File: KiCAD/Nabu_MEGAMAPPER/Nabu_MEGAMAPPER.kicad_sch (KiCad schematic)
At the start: 14 parts, among them J1 Z80 Socket Header, J2 Z80 Socket Header, U1 Z80CPU, U10 74LS374, U11 GAL22V10, U12 GAL22V10, U2 AS6C4008-55PCN, U3 74LS670, U4 74LS670, U5 HM6116, U6 74LS157, U7 74LS157, U8 74LS157, U9 74LS244

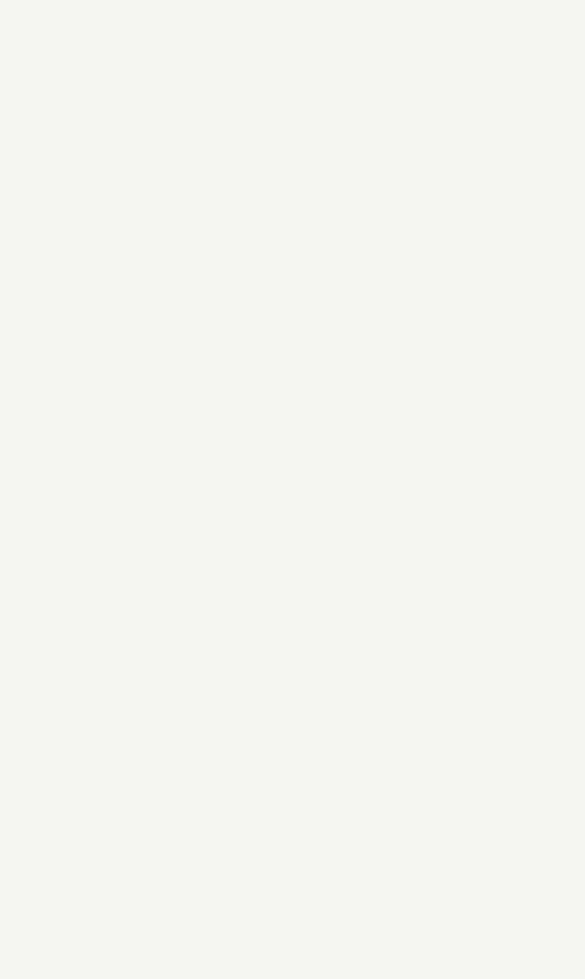
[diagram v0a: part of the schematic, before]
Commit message: Removed some of the 22V10s in favor of a CPLD
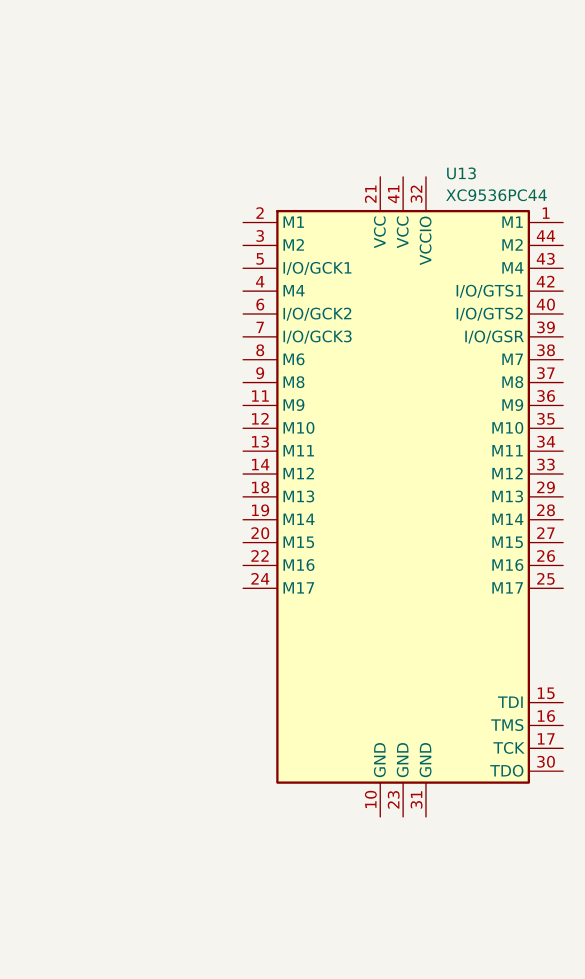
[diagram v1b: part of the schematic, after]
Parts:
- added U13: XC9536PC44, symbol CPLD_Xilinx:XC9536PC44
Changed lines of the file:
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@@
+    )
+  )
+  (symbol (lib_id "CPLD_Xilinx:XC9536PC44") (at 288.29 132.715 0) (unit 1)
+    (in_bom yes) (on_board yes) (dnp no) (fields_autoplaced)
+    (property "Reference" "U13" (at 293.0241 96.8207 0)
+      (effects (font (size 1.27 1.27)) (justify left))
+    )
+    (property "Value" "XC9536PC44" (at 293.0241 99.2449 0)
+      (effects (font (size 1.27 1.27)) (justify left))
+    )
+    (property "Footprint" "" (at 288.29 132.715 0)
+      (effects (font (size 1.27 1.27)) hide)
+    )
+    (property "Datasheet" "xilinx/xc9536.pdf" (at 288.29 132.715 0)
+      (effects (font (size 1.27 1.27)) hide)
+    )
+    (pin "1")
+    (pin "10")
+    (pin "11")
+    (pin "12")
+    (pin "13")
+    (pin "14")
+    (pin "15")
+    (pin "16")
+    (pin "17")
+    (pin "18")
+    (pin "19")
+    (pin "2")
+    (pin "20")
+    (pin "21")
+    (pin "22")
+    (pin "23")
+    (pin "24")
+    (pin "25")
+    (pin "26")
+    (pin "27")
+    (pin "28")
+    (pin "29")
+    (pin "3")
+    (pin "30")
+    (pin "31")
+    (pin "32")
+    (pin "33")
+    (pin "34")
+    (pin "35")
+    (pin "36")
+    (pin "37")
+    (pin "38")
+    (pin "39")
+    (pin "4")
+    (pin "40")
+    (pin "41")
+    (pin "42")
+    (pin "43")
+    (pin "44")
+    (pin "5")
+    (pin "6")
+    (pin "7")
+    (pin "8")
+    (pin "9")
+    (instances
+      (project "Nabu_MEGAMAPPER"
+        (path "/08a88c4b-5d36-43ed-bafe-b5ff1ee4c2dd"
+          (reference "U13") (unit 1)
+        )
+      )
     )
   )

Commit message: Continued work on schematic
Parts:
- removed U11, U12: GAL22V10, symbol Custom:GAL22V10
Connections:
- net *IORQ: now also U13.3 (M2)
- net *M1: now also U13.5 (I/O/GCK1)
- net *MREQ: now also U13.2 (M1)
- net *RESET: now also U13.39 (I/O/GSR)
- net +5V: now also U13.21 (VCC), U13.32 (VCCIO), U13.41 (VCC)
- net A10: now also U10.7 (D2)
- net A11: now also U10.8 (D3)
- net A12: now also U10.13 (D4)
- net A13: now also U10.14 (D5)
- net A14: now also U10.17 (D6)
- net A15: now also U10.18 (D7)
- net A8: now also U10.3 (D0)
- net A9: now also U10.4 (D1)
- net D0: now also U13.12 (M10); no longer U10.3 (D0)
- net D1: now also U13.13 (M11); no longer U10.4 (D1)
- net D2: now also U13.14 (M12); no longer U10.7 (D2)
- net D3: now also U13.18 (M13); no longer U10.8 (D3)
- net D4: now also U13.19 (M14); no longer U10.13 (D4)
- net D5: now also U13.20 (M15); no longer U10.14 (D5)
- net D6: now also U13.22 (M16); no longer U10.17 (D6)
- net D7: now also U13.24 (M17); no longer U10.18 (D7)
- net GND: now also U13.10 (GND), U13.23 (GND), U13.31 (GND)
- net *BNK_WR: now reaches U4.12 (~{Ew})
- net *BNK_WR: now also U3.12 (~{Ew})
- net *UA_OE: now reaches U10.1 (OE)
- net UA_CLK: now reaches U10.11 (Cp)
- net TRAP renamed A_TRAP
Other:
- moved on the sheet: U13

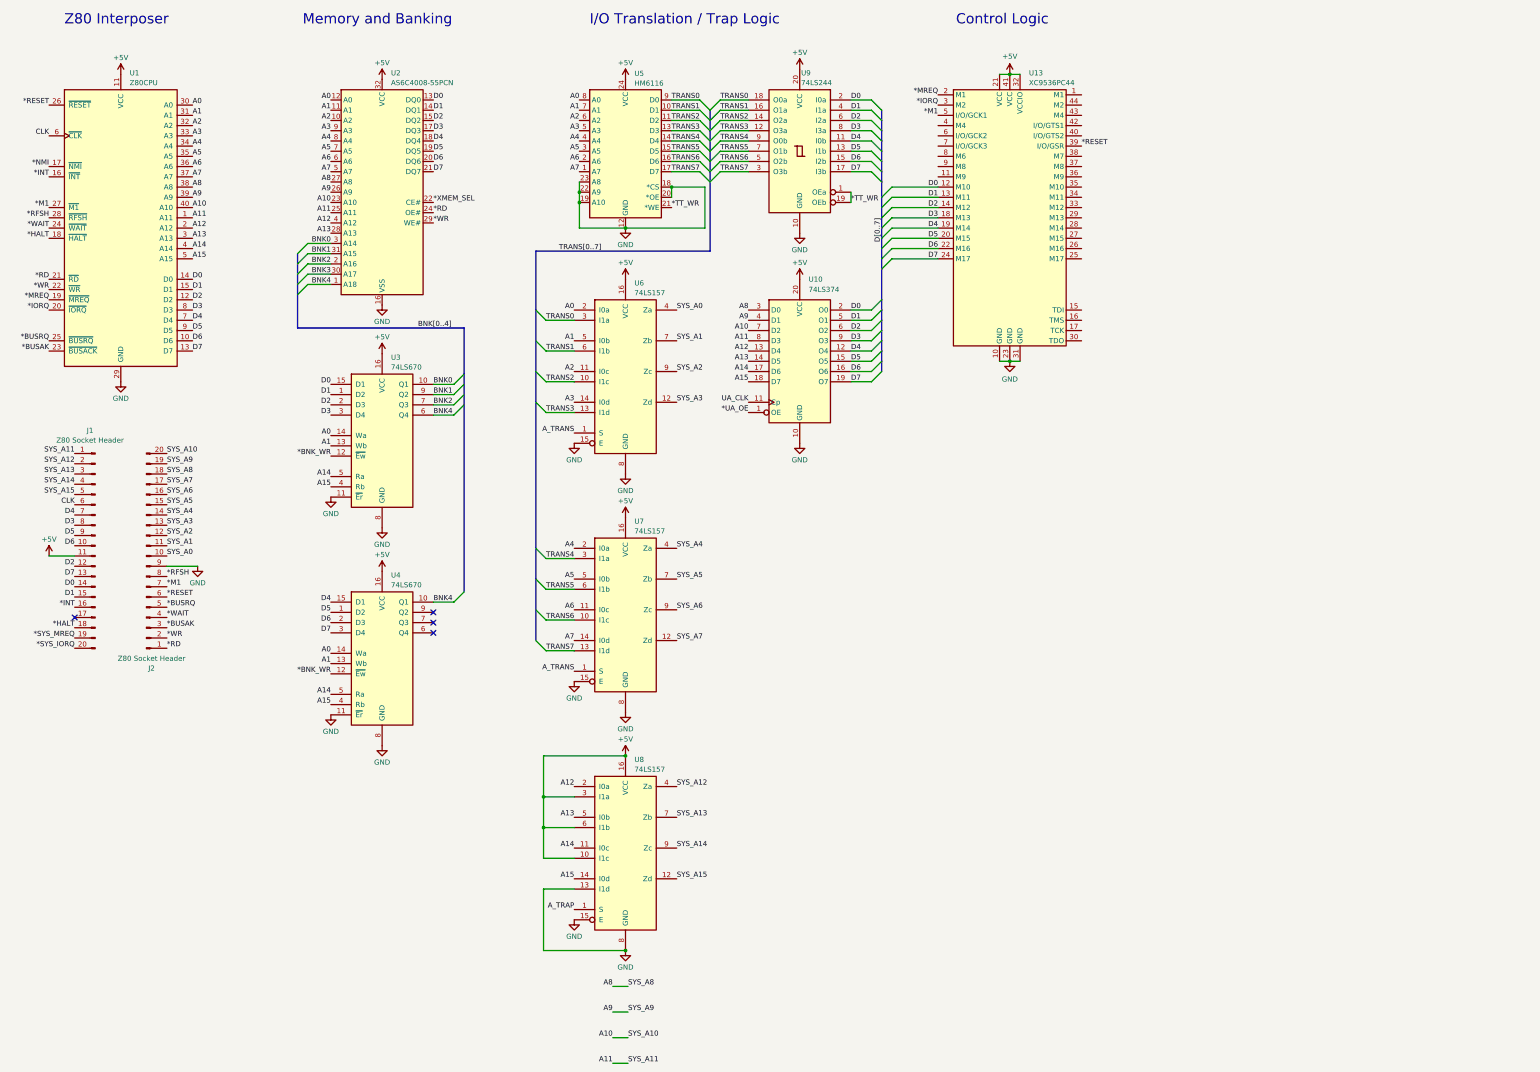
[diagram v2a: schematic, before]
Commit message: Added full address capture logic to schematic
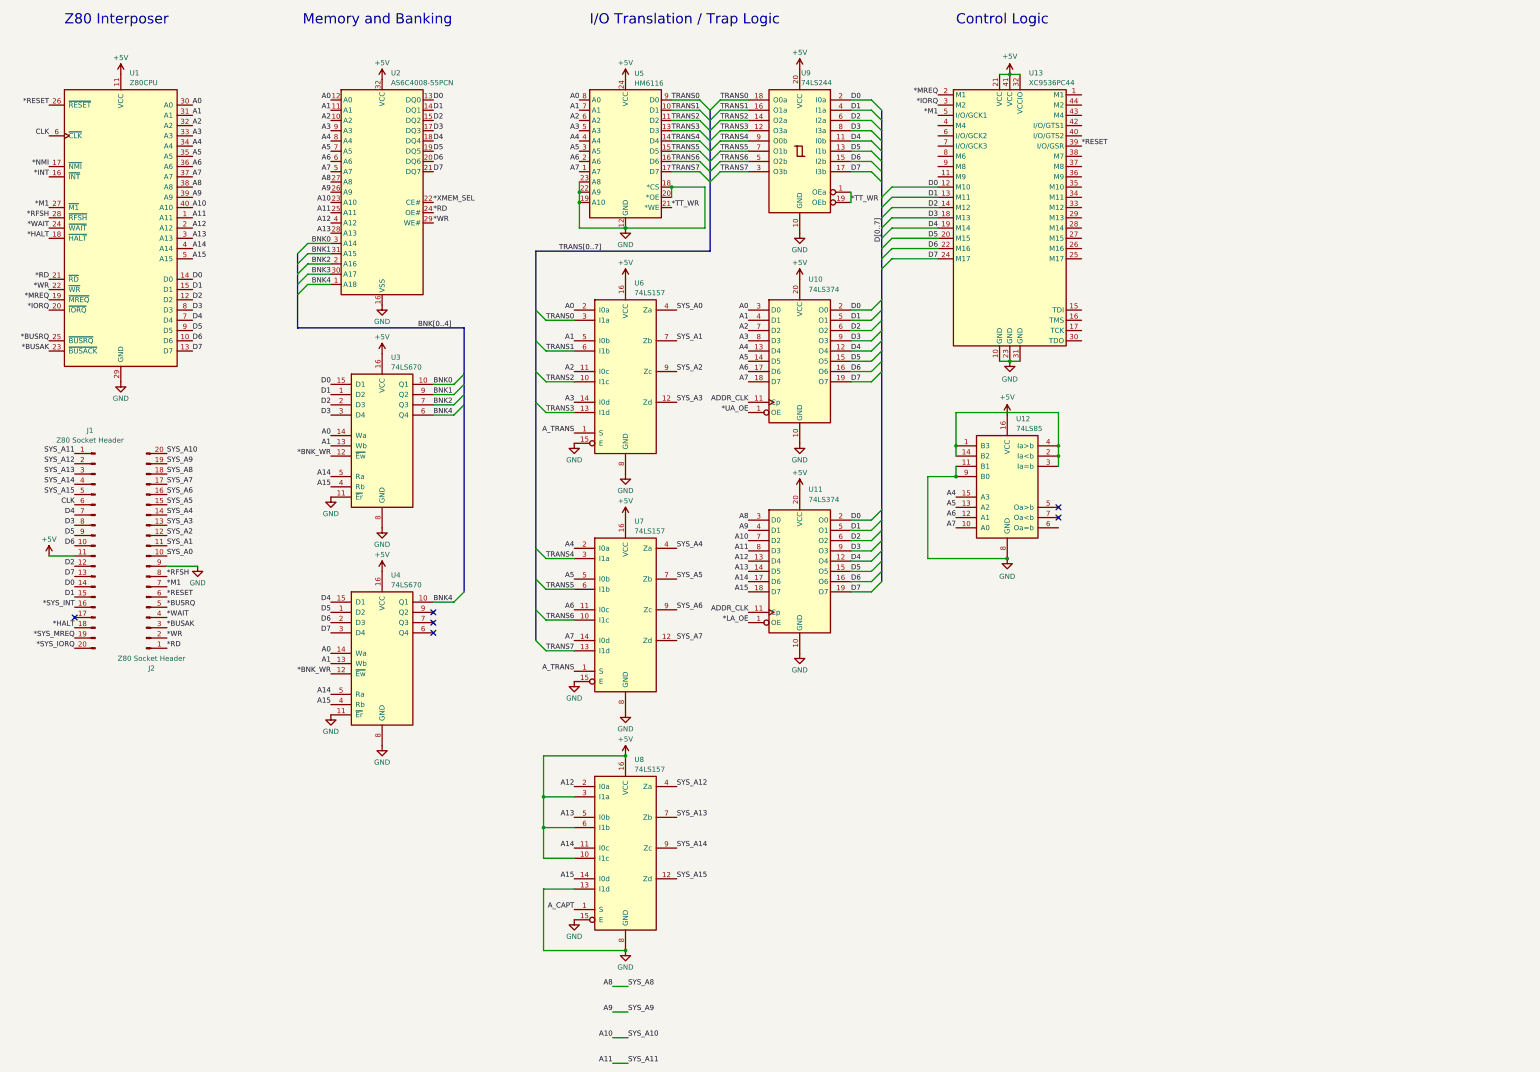
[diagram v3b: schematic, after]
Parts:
- added U11: 74LS374, symbol 74xx:74LS374
- added U12: 74LS85, symbol 74xx:74LS85
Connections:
- net *INT: no longer J1.16 (Pin_16)
- net +5V: now also U11.20 (VCC), U12.16 (VCC)
- net A0: now also U10.3 (D0)
- net A1: now also U10.4 (D1)
- net A10: now also U11.7 (D2); no longer U10.7 (D2)
- net A11: now also U11.8 (D3); no longer U10.8 (D3)
- net A12: now also U11.13 (D4); no longer U10.13 (D4)
- net A13: now also U11.14 (D5); no longer U10.14 (D5)
- net A14: now also U11.17 (D6); no longer U10.17 (D6)
- net A15: now also U11.18 (D7); no longer U10.18 (D7)
- net A2: now also U10.7 (D2)
- net A3: now also U10.8 (D3)
- net A4: now also U10.13 (D4), U12.15 (A3)
- net A5: now also U10.14 (D5), U12.13 (A2)
- net A6: now also U10.17 (D6), U12.12 (A1)
- net A7: now also U10.18 (D7), U12.10 (A0)
- net A8: now also U11.3 (D0); no longer U10.3 (D0)
- net A9: now also U11.4 (D1); no longer U10.4 (D1)
- net D0: now also U11.2 (O0)
- net D1: now also U11.5 (O1)
- net D2: now also U11.6 (O2)
- net D3: now also U11.9 (O3)
- net D4: now also U11.12 (O4)
- net D5: now also U11.15 (O5)
- net D6: now also U11.16 (O6)
- net D7: now also U11.19 (O7)
- net GND: now also U11.10 (GND), U12.11 (B1), U12.8 (GND), U12.9 (B0)
- net A_TRAP renamed A_CAPT
- net UA_CLK renamed ADDR_CLK
- net ADDR_CLK: now also U11.11 (Cp)
- new net: U12.1 (B3), U12.14 (B2), U12.2 (Ia<b), U12.3 (Ia=b), U12.4 (Ia>b)
- new net *LA_OE: U11.1 (OE)
- new net *SYS_INT: J1.16 (Pin_16)
- no-connect marks 4 -> 6
